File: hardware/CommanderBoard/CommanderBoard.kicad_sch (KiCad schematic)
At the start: 37 parts, among them J1 Conn_01x22, J1BUS1 Conn_02x04_Odd_Even, J1BUS2 Conn_02x04_Odd_Even, J2 Conn_01x22, J2BUS1 Conn_01x02, J2BUS2 Conn_01x02, J3 HUB75, SW1 SW_SPDT, SW2 SW_DP3T, SW3 SW_DP3T, SW4 SW_DPDT_x2

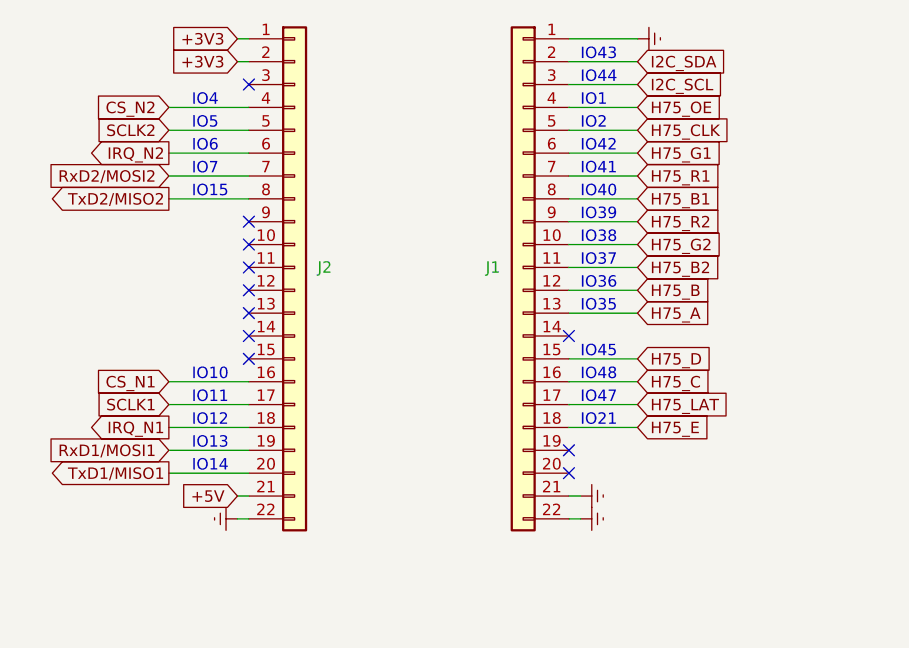
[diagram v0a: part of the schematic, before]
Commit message: Reworked Commanderboard, horizontal orientation of the ESP32-S3.
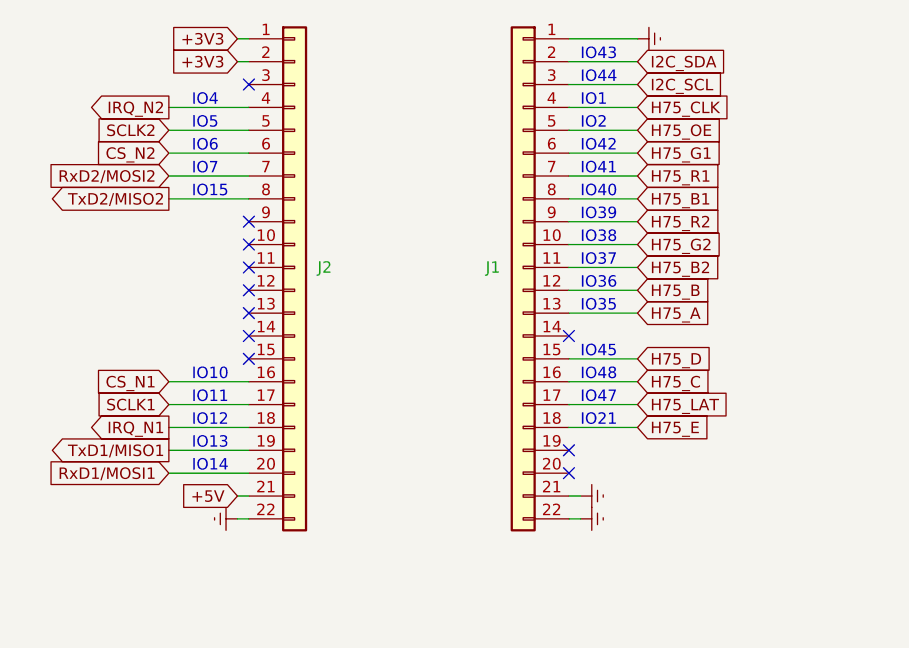
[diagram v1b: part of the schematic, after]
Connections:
- net CS_N2: now also J2.6 (Pin_6); no longer J2.4 (Pin_4)
- net H75_CLK: now also J1.4 (Pin_4); no longer J1.5 (Pin_5)
- net H75_OE: now also J1.5 (Pin_5); no longer J1.4 (Pin_4)
- net IRQ_N2: now also J2.4 (Pin_4); no longer J2.6 (Pin_6)
- net RxD1/MOSI1: now also J2.20 (Pin_20); no longer J2.19 (Pin_19)
- net TxD1/MISO1: now also J2.19 (Pin_19); no longer J2.20 (Pin_20)
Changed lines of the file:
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@@
 	(wire
 		(pts
-			(xy 63.5 31.75) (xy 72.39 31.75)
+			(xy 115.57 31.75) (xy 107.95 31.75)
 		)
 		(stroke
@@
 	(wire
 		(pts
-			(xy 163.83 93.98) (xy 163.83 92.71)
+			(xy 63.5 31.75) (xy 72.39 31.75)
 		)
 		(stroke
@@
 	(wire
 		(pts
-			(xy 107.95 41.91) (xy 115.57 41.91)
+			(xy 163.83 93.98) (xy 163.83 92.71)
 		)
 		(stroke
@@
 	(wire
 		(pts
-			(xy 173.99 86.36) (xy 175.26 86.36)
+			(xy 63.5 34.29) (xy 72.39 34.29)
 		)
 		(stroke
@@
 	(wire
 		(pts
-			(xy 63.5 69.85) (xy 72.39 69.85)
+			(xy 107.95 41.91) (xy 115.57 41.91)
 		)
 		(stroke
@@
 	(wire
 		(pts
-			(xy 186.69 91.44) (xy 184.15 91.44)
+			(xy 173.99 86.36) (xy 175.26 86.36)
 		)
 		(stroke
@@
 	(wire
 		(pts
-			(xy 231.14 44.45) (xy 232.41 44.45)
+			(xy 186.69 91.44) (xy 184.15 91.44)
 		)
 		(stroke
@@
 	(wire
 		(pts
-			(xy 210.82 88.9) (xy 212.09 88.9)
+			(xy 231.14 44.45) (xy 232.41 44.45)
 		)
 		(stroke
@@
 	(wire
 		(pts
-			(xy 107.95 29.21) (xy 115.57 29.21)
+			(xy 210.82 88.9) (xy 212.09 88.9)
 		)
 		(stroke
@@
 	(wire
 		(pts
-			(xy 63.5 29.21) (xy 72.39 29.21)
-		)
-		(stroke
-			(width 0)
-			(type default)
-		)
-	)
-	(wire
-		(pts
 			(xy 175.26 72.39) (xy 176.53 72.39)
 		)
@@
 	(wire
 		(pts
-			(xy 63.5 34.29) (xy 72.39 34.29)
-		)
-		(stroke
-			(width 0)
-			(type default)
-		)
-	)
-	(wire
-		(pts
 			(xy 227.33 142.24) (xy 228.6 142.24)
 		)
@@
 	(wire
 		(pts
-			(xy 231.14 49.53) (xy 232.41 49.53)
+			(xy 115.57 29.21) (xy 107.95 29.21)
 		)
 		(stroke
@@
 	(wire
 		(pts
-			(xy 195.58 96.52) (xy 200.66 96.52)
+			(xy 231.14 49.53) (xy 232.41 49.53)
 		)
 		(stroke
@@
 	(wire
 		(pts
-			(xy 107.95 31.75) (xy 115.57 31.75)
+			(xy 195.58 96.52) (xy 200.66 96.52)
 		)
 		(stroke
@@
 	(wire
 		(pts
-			(xy 63.5 67.31) (xy 72.39 67.31)
+			(xy 227.33 132.08) (xy 228.6 132.08)
 		)
 		(stroke
@@
 	(wire
 		(pts
-			(xy 227.33 132.08) (xy 228.6 132.08)
+			(xy 186.69 86.36) (xy 187.96 86.36)
 		)
 		(stroke
@@
 	(wire
 		(pts
-			(xy 186.69 86.36) (xy 187.96 86.36)
+			(xy 107.95 46.99) (xy 115.57 46.99)
 		)
 		(stroke
@@
 	(wire
 		(pts
-			(xy 107.95 46.99) (xy 115.57 46.99)
+			(xy 200.66 88.9) (xy 210.82 88.9)
 		)
 		(stroke
@@
 	(wire
 		(pts
-			(xy 200.66 88.9) (xy 210.82 88.9)
+			(xy 229.87 95.25) (xy 237.49 95.25)
 		)
 		(stroke
@@
 	(wire
 		(pts
-			(xy 229.87 95.25) (xy 237.49 95.25)
+			(xy 172.72 40.64) (xy 171.45 40.64)
 		)
 		(stroke
@@
 	(wire
 		(pts
-			(xy 172.72 40.64) (xy 171.45 40.64)
+			(xy 63.5 29.21) (xy 72.39 29.21)
 		)
 		(stroke
@@
 	(wire
 		(pts
+			(xy 63.5 67.31) (xy 72.39 67.31)
+		)
+		(stroke
+			(width 0)
+			(type default)
+		)
+	)
+	(wire
+		(pts
 			(xy 186.69 50.8) (xy 185.42 50.8)
 		)
@@
 	(wire
 		(pts
+			(xy 63.5 69.85) (xy 72.39 69.85)
+		)
+		(stroke
+			(width 0)
+			(type default)
+		)
+	)
+	(wire
+		(pts
 			(xy 186.69 35.56) (xy 185.42 35.56)
 		)
@@
 	(global_label "H75_OE"
 		(shape input)
-		(at 115.57 29.21 0)
+		(at 115.57 31.75 0)
 		(fields_autoplaced yes)
 		(effects
@@
 		)
 		(property "Intersheetrefs" "${INTERSHEET_REFS}"
-			(at 125.7518 29.21 0)
+			(at 125.7518 31.75 0)
 			(effects
 				(font
@@
 	(global_label "H75_CLK"
 		(shape input)
-		(at 115.57 31.75 0)
+		(at 115.57 29.21 0)
 		(fields_autoplaced yes)
 		(effects
@@
 		)
 		(property "Intersheetrefs" "${INTERSHEET_REFS}"
-			(at 126.8404 31.75 0)
+			(at 126.8404 29.21 0)
 			(effects
 				(font
@@
 	(global_label "IRQ_N2"
 		(shape output)
-		(at 63.5 34.29 180)
+		(at 63.5 29.21 180)
 		(fields_autoplaced yes)
 		(effects
@@
 		)
 		(property "Intersheetrefs" "${INTERSHEET_REFS}"
-			(at 53.8019 34.29 0)
+			(at 53.8019 29.21 0)
 			(effects
 				(font
@@
 	(global_label "TxD1/MISO1"
 		(shape output)
-		(at 63.5 69.85 180)
+		(at 63.5 67.31 180)
 		(fields_autoplaced yes)
 		(effects
@@
 		)
 		(property "Intersheetrefs" "${INTERSHEET_REFS}"
-			(at 48.9034 69.85 0)
+			(at 48.9034 67.31 0)
 			(effects
 				(font
@@
 	(global_label "RxD1/MOSI1"
 		(shape input)
-		(at 63.5 67.31 180)
+		(at 63.5 69.85 180)
 		(fields_autoplaced yes)
 		(effects
@@
 		)
 		(property "Intersheetrefs" "${INTERSHEET_REFS}"
-			(at 48.601 67.31 0)
+			(at 48.601 69.85 0)
 			(effects
 				(font
@@
 	(global_label "CS_N2"
 		(shape input)
-		(at 63.5 29.21 180)
+		(at 63.5 34.29 180)
 		(fields_autoplaced yes)
 		(effects
@@
 		)
 		(property "Intersheetrefs" "${INTERSHEET_REFS}"
-			(at 54.5277 29.21 0)
+			(at 54.5277 34.29 0)
 			(effects
 				(font

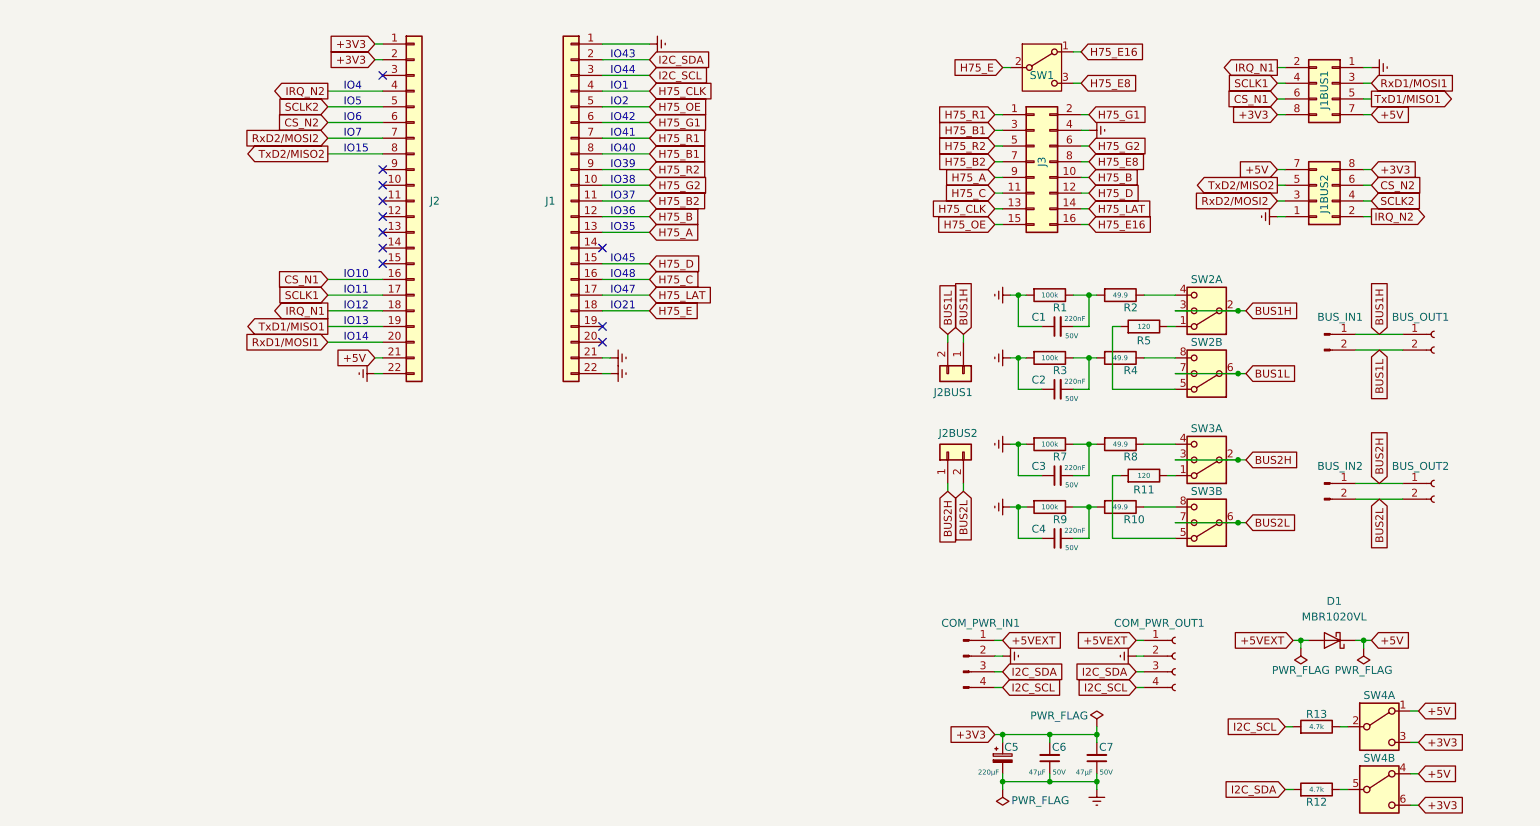
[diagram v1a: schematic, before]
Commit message: Added two joysticks to CommanderBoard.
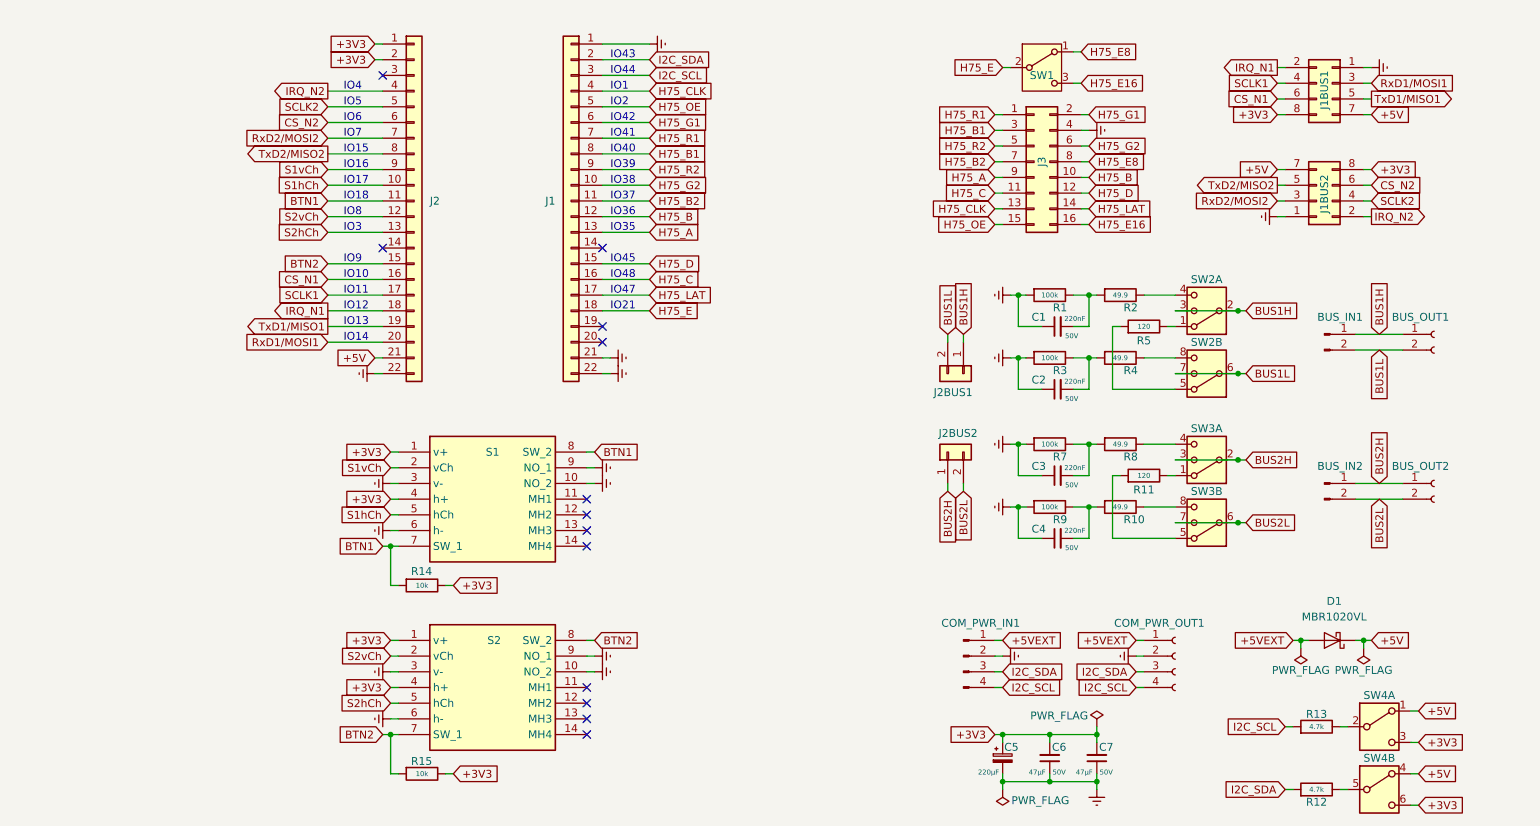
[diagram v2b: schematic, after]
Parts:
- added R14, R15: 10k, Resistor_SMD:R_1206_3216Metric, symbol Device:R
- added S1, S2: THB001P, THB001P, symbol THB001P:THB001P
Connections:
- net +3V3: now also R14.1, R15.1, S1.1 (v+), S1.4 (h+), S2.1 (v+), S2.4 (h+)
- net GNDREF: now also S1.10 (NO_2), S1.3 (v-), S1.6 (h-), S1.9 (NO_1), S2.10 (NO_2), S2.3 (v-), S2.6 (h-), S2.9 (NO_1)
- net H75_E16: now also SW1.3 (C); no longer SW1.1 (A)
- net H75_E8: now also SW1.1 (A); no longer SW1.3 (C)
- net S1hCh: now reaches J2.10 (Pin_10)
- net S1hCh: now also S1.5 (hCh)
- net BTN1: now reaches J2.11 (Pin_11)
- net BTN1: now also R14.2, S1.7 (SW_1), S1.8 (SW_2)
- net S2vCh: now reaches J2.12 (Pin_12)
- net S2vCh: now also S2.2 (vCh)
- net S2hCh: now reaches J2.13 (Pin_13)
- net S2hCh: now also S2.5 (hCh)
- net BTN2: now reaches J2.15 (Pin_15)
- net BTN2: now also R15.2, S2.7 (SW_1), S2.8 (SW_2)
- net S1vCh: now reaches J2.9 (Pin_9)
- net S1vCh: now also S1.2 (vCh)
- no-connect marks 11 -> 13
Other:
- note added: "IO16"
- note added: "IO17"
- note added: "IO18"
- note added: "IO3"
- note added: "IO8"
- note added: "IO9"

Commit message: Added software for thumbstick test.
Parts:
- S1, S2: footprint THB001P -> LIB_THB001P:THB001P
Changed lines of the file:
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@@
 			)
 		)
-		(property "Footprint" "THB001P"
+		(property "Footprint" "LIB_THB001P:THB001P"
 			(at 101.6 182.55 0)
 			(effects
@@
 			)
 		)
-		(property "Footprint" "THB001P"
+		(property "Footprint" "LIB_THB001P:THB001P"
 			(at 101.6 213.03 0)
 			(effects

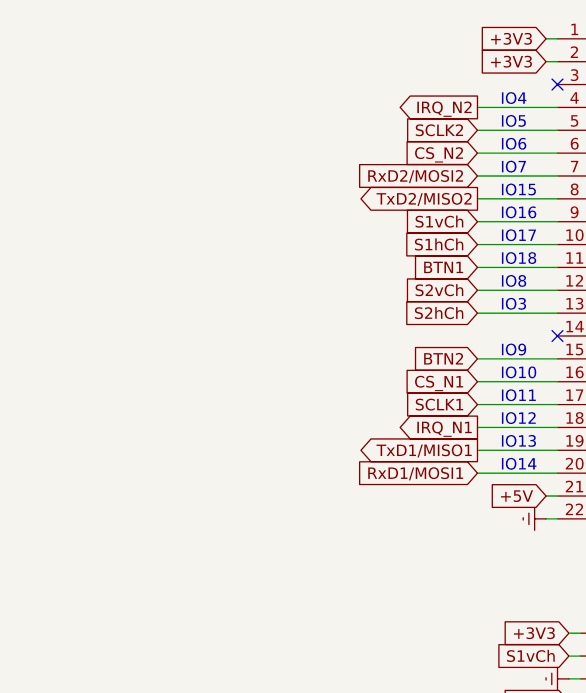
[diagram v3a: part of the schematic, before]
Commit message: Gave thumbstuck #1 a bit more space.
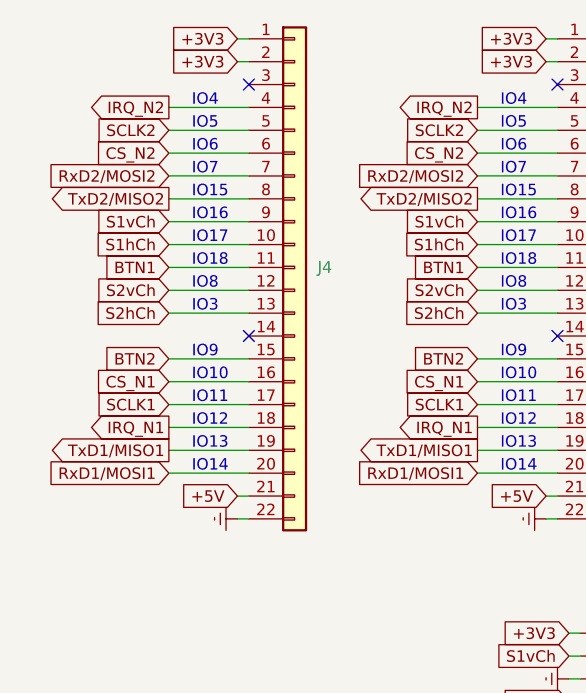
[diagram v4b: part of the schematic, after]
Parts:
- added J4: Conn_01x22, Connector_PinSocket_2.54mm:PinSocket_1x22_P2.54mm_Vertical, symbol Connector_Generic:Conn_01x22
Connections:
- net +3V3: now also J4.1 (Pin_1), J4.2 (Pin_2)
- net +5V: now also J4.21 (Pin_21)
- net BTN1: now also J4.11 (Pin_11)
- net BTN2: now also J4.15 (Pin_15)
- net CS_N1: now also J4.16 (Pin_16)
- net CS_N2: now also J4.6 (Pin_6)
- net GNDREF: now also J4.22 (Pin_22)
- net IRQ_N1: now also J4.18 (Pin_18)
- net IRQ_N2: now also J4.4 (Pin_4)
- net RxD1/MOSI1: now also J4.20 (Pin_20)
- net RxD2/MOSI2: now also J4.7 (Pin_7)
- net S1hCh: now also J4.10 (Pin_10)
- net S1vCh: now also J4.9 (Pin_9)
- net S2hCh: now also J4.13 (Pin_13)
- net S2vCh: now also J4.12 (Pin_12)
- net SCLK1: now also J4.17 (Pin_17)
- net SCLK2: now also J4.5 (Pin_5)
- net TxD1/MISO1: now also J4.19 (Pin_19)
- net TxD2/MISO2: now also J4.8 (Pin_8)
- no-connect marks 13 -> 15

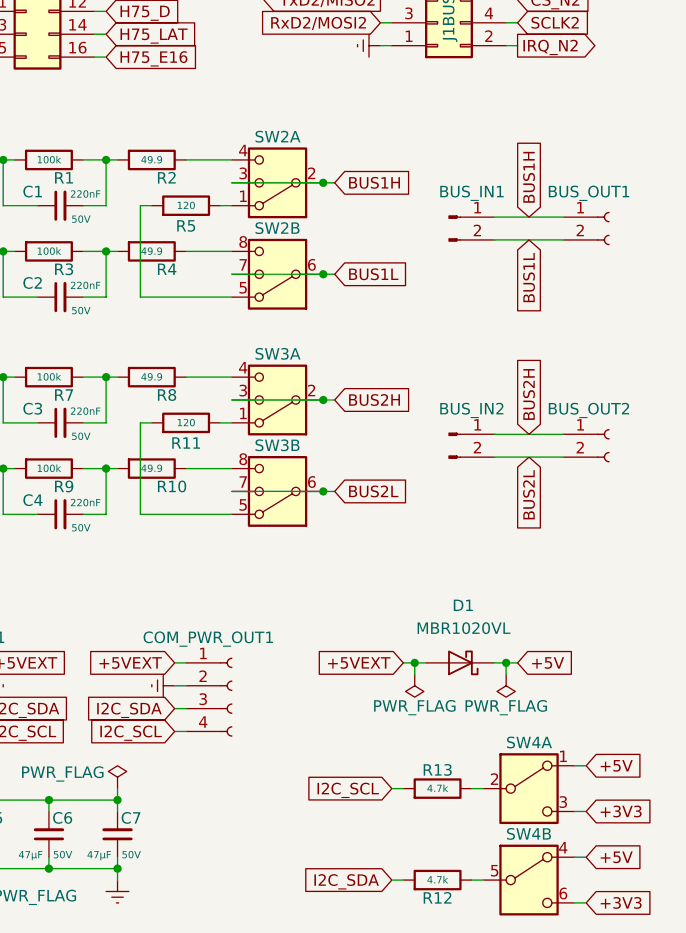
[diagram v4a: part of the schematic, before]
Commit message: Added I2C passthrough (listener) mode.
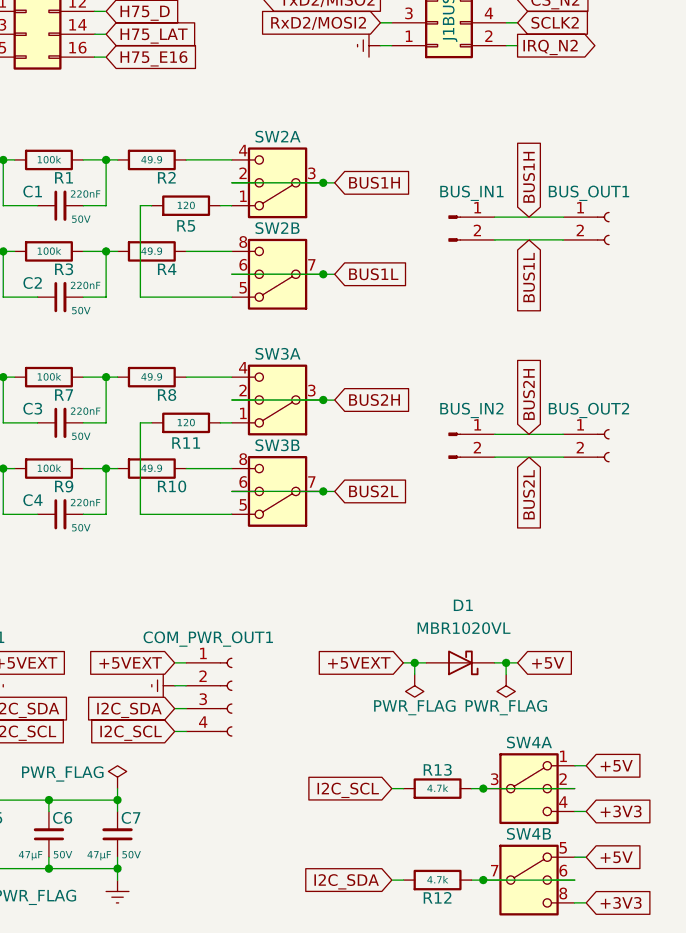
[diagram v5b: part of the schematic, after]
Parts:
- SW4: value SW_DPDT_x2 -> SW_DP3T; footprint LIB_CL-SB-22B-01T:CLSB22B01T -> LIB_CL-SB-23B-01T:CLSB23B01T; symbol Switch:SW_DPDT_x2 -> Switch:SW_DP3T
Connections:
- net +3V3: now also SW4.4, SW4.8; no longer SW4.3 (C), SW4.6 (C)
- net +5V: now also SW4.5; no longer SW4.4 (A)
- net at R13.1, SW4.2: now also SW4.3
- net at R12.1: now also SW4.6, SW4.7; no longer SW4.5 (B)
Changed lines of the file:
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@@
 	)
 	(junction
+		(at 228.6 142.24)
+		(diameter 0)
+		(color 0 0 0 0)
+	)
+	(junction
+		(at 228.6 132.08)
+		(diameter 0)
+		(color 0 0 0 0)
+	)
+	(junction
 		(at 186.69 86.36)
 		(diameter 0)
@@
 	(wire
 		(pts
+			(xy 228.6 132.08) (xy 238.76 132.08)
+		)
+		(stroke
+			(width 0)
+			(type default)
+		)
+	)
+	(wire
+		(pts
 			(xy 71.12 74.93) (xy 72.39 74.93)
 		)
@@
 	(wire
 		(pts
+			(xy 228.6 142.24) (xy 238.76 142.24)
+		)
+		(stroke
+			(width 0)
+			(type default)
+		)
+	)
+	(wire
+		(pts
 			(xy 107.95 62.23) (xy 115.57 62.23)
 		)
@@
 	)
 	(symbol
-		(lib_name "SW_DP3T_1")
 		(lib_id "Switch:SW_DP3T")
 		(at 205.74 64.77 180)
@@
 	)
 	(symbol
-		(lib_id "Switch:SW_DPDT_x2")
+		(lib_name "SW_DP3T_5")
+		(lib_id "Switch:SW_DP3T")
 		(at 233.68 142.24 0)
 		(unit 2)
@@
 			)
 		)
-		(property "Value" "SW_DPDT_x2"
+		(property "Value" "SW_DP3T"
 			(at 233.68 135.89 0)
 			(effects
@@
 			)
 		)
-		(property "Footprint" "LIB_CL-SB-22B-01T:CLSB22B01T"
-			(at 233.68 142.24 0)
+		(property "Footprint" "LIB_CL-SB-23B-01T:CLSB23B01T"
+			(at 217.805 137.795 0)
 			(effects
 				(font
@@
 		)
 		(property "Datasheet" "~"
-			(at 233.68 142.24 0)
+			(at 217.805 137.795 0)
 			(effects
 				(font
@@
 			)
 		)
-		(property "Description" "Switch, dual pole double throw, separate symbols"
+		(property "Description" "Switch, three position, dual pole triple throw, 3 position switch, SP3T"
 			(at 233.68 142.24 0)
 			(effects
@@
 		(pin "1"
 		)
+		(pin "8"
+		)
+		(pin "7"
+		)
 		(instances
 			(project ""
@@
 	)
 	(symbol
-		(lib_name "SW_DP3T_3")
 		(lib_id "Switch:SW_DP3T")
 		(at 205.74 99.06 180)
@@
 	)
 	(symbol
-		(lib_id "Switch:SW_DPDT_x2")
+		(lib_name "SW_DP3T_4")
+		(lib_id "Switch:SW_DP3T")
 		(at 233.68 132.08 0)
 		(unit 1)
@@
 			)
 		)
-		(property "Value" "SW_DPDT_x2"
+		(property "Value" "SW_DP3T"
 			(at 233.68 125.73 0)
 			(effects
@@
 			)
 		)
-		(property "Footprint" "LIB_CL-SB-22B-01T:CLSB22B01T"
-			(at 233.68 132.08 0)
+		(property "Footprint" "LIB_CL-SB-23B-01T:CLSB23B01T"
+			(at 217.805 127.635 0)
 			(effects
 				(font
@@
 		)
 		(property "Datasheet" "~"
-			(at 233.68 132.08 0)
+			(at 217.805 127.635 0)
 			(effects
 				(font
@@
 			)
 		)
-		(property "Description" "Switch, dual pole double throw, separate symbols"
+		(property "Description" "Switch, three position, dual pole triple throw, 3 position switch, SP3T"
 			(at 233.68 132.08 0)
 			(effects
@@
 		(pin "1"
 		)
+		(pin "8"
+		)
+		(pin "7"
+		)
 		(instances
 			(project ""
@@
 	)
 	(symbol
-		(lib_name "SW_DP3T_2")
 		(lib_id "Switch:SW_DP3T")
 		(at 205.74 74.93 180)
